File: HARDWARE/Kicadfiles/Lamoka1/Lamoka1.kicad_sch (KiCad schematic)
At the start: 8 parts, among them J1 2606-1108/010-000, J2 2606-1352, J3 USB_C_Receptacle_USB2.0_14P, J4 470531000, J5 2604-1103, J6 Male-Header, J7 Male-Header

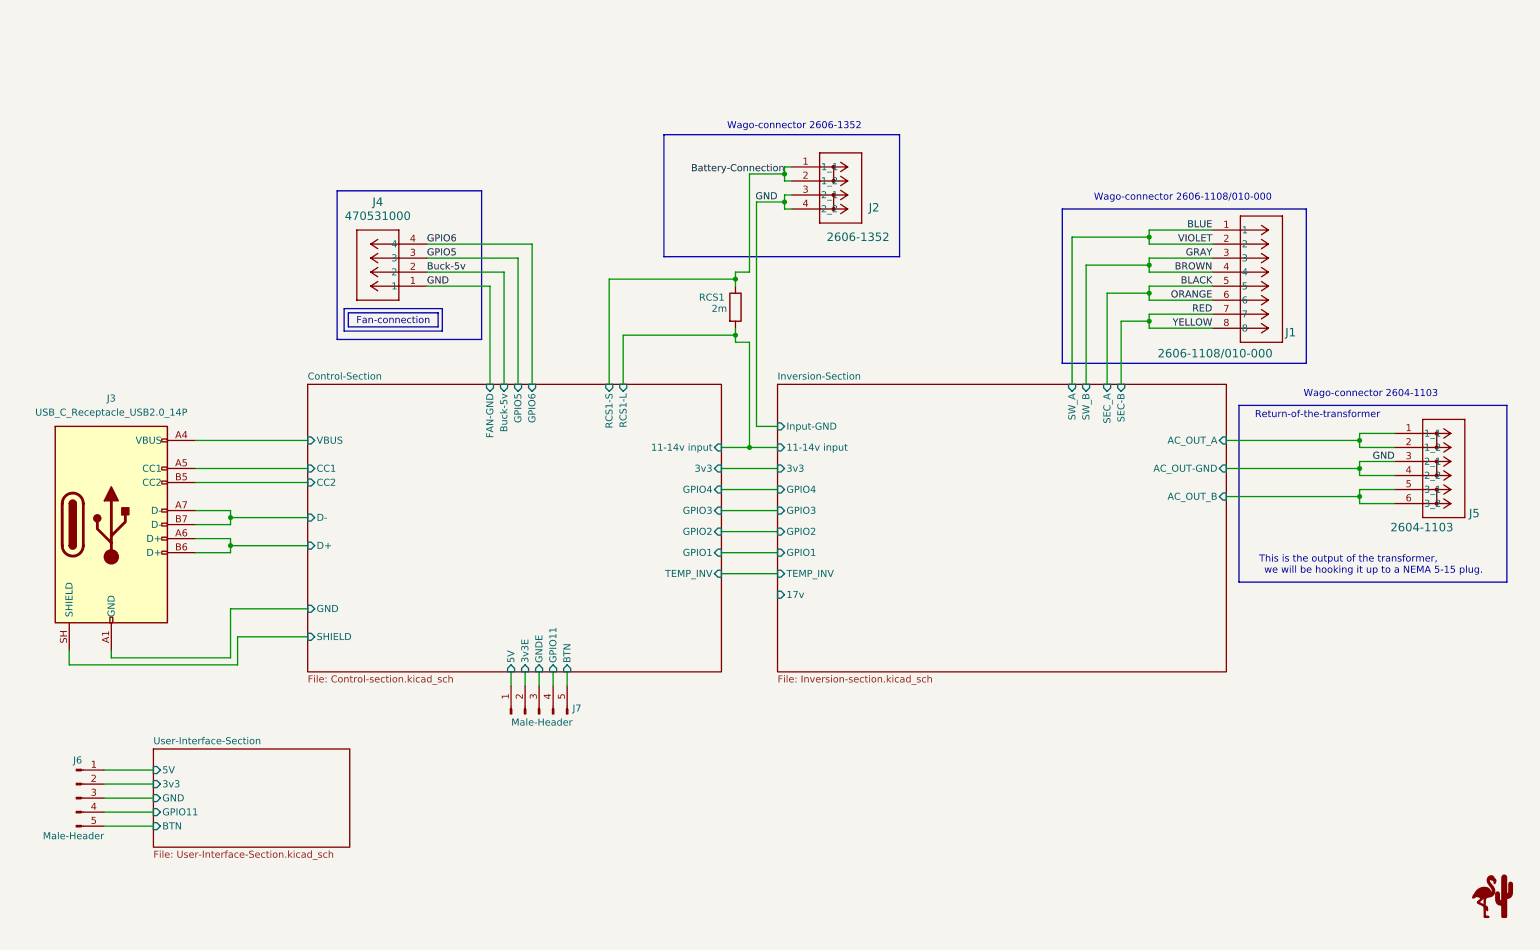
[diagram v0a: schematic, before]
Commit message: ADD H bridge section, tighten everything in PCB routing to be neater. ADD mounting holes M3, etc
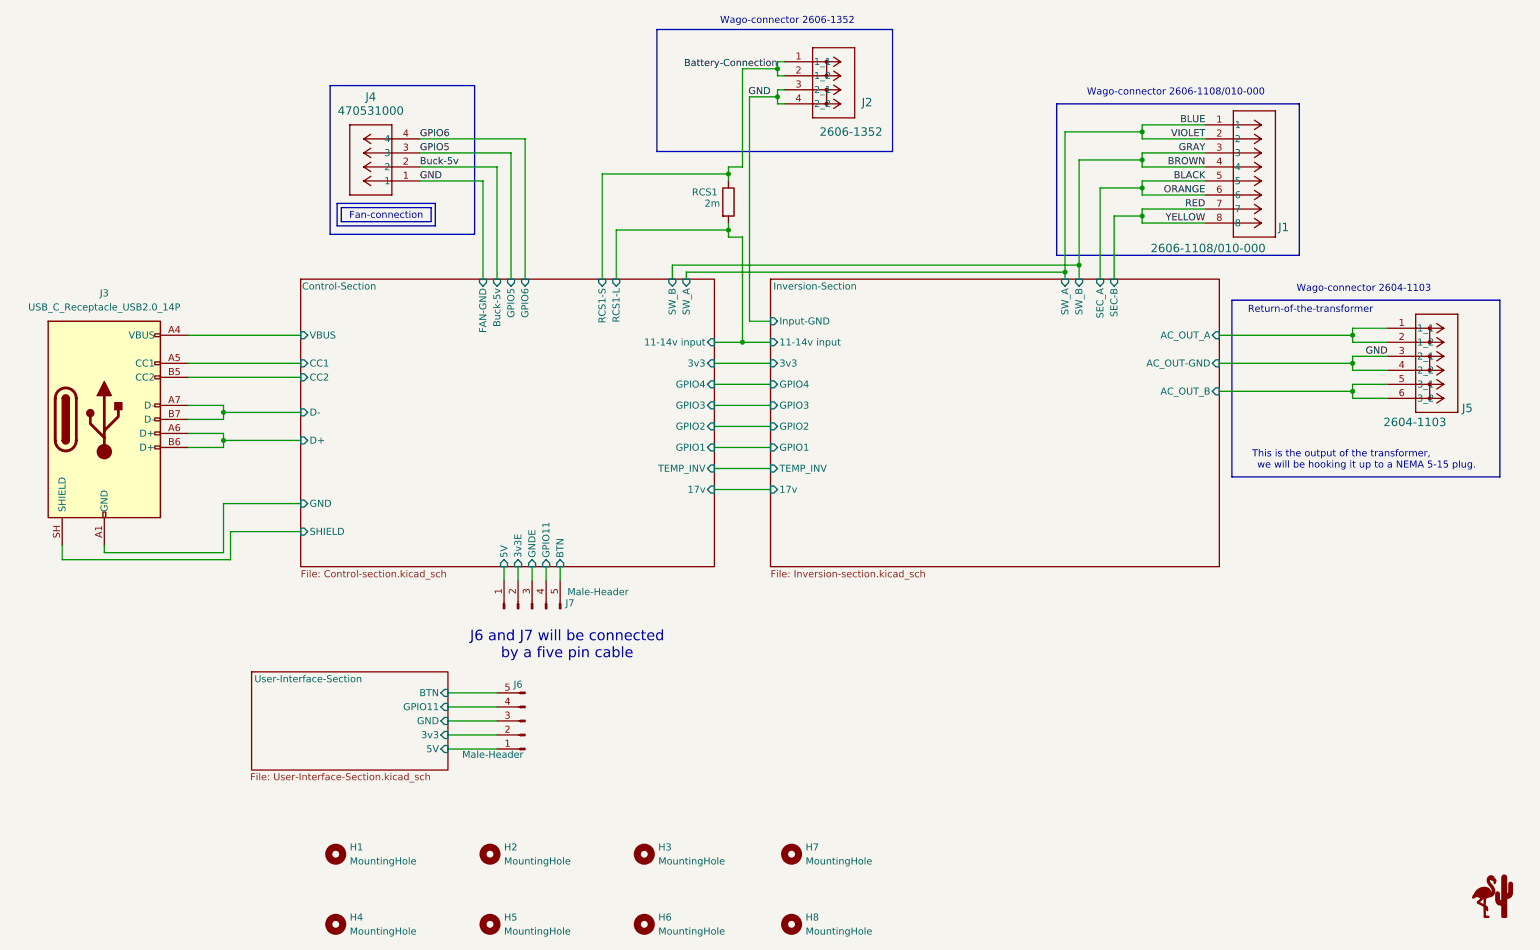
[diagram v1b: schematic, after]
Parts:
- added H1, H2, H3, H4, H5, H6, H7, H8: MountingHole, MountingHole:MountingHole_3.2mm_M3, symbol Mechanical:MountingHole
- J4: footprint 470531000:CONN_SD-47053-001_H10p00_MOL -> Connector:FanPinHeader_1x04_P2.54mm_Vertical
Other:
- sheet Control-Section ports: added 17v, SW_A, SW_B; removed none
- note added: "J6 and J7 will be connected by a five pin cable"
- moved on the sheet: J1, J2, J3, J4, J5, J6, J7, RCS1

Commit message: Get DRC down all the way, other misc improvements
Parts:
- H1, H2, H3, H4, H5, H6, H7, H8: KiLib_Generator (none) -> mounting_hardware/mounting_hole
- J6, J7: KiLib_Generator (none) -> connector/pin_header_socket
- RCS1: KiLib_Generator (none) -> SMD_2terminal_chip_molded
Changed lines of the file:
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@@
+			)
+		)
+		(property "KiLib_Generator" "mounting_hardware/mounting_hole"
+			(at 69.85 167.64 0)
+			(hide yes)
+			(show_name no)
+			(do_not_autoplace no)
+			(effects
+				(font
+					(size 1.27 1.27)
+				)
 			)
 		)
@@
 			)
 		)
+		(property "KiLib_Generator" "mounting_hardware/mounting_hole"
+			(at 152.4 167.64 0)
+			(hide yes)
+			(show_name no)
+			(do_not_autoplace no)
+			(effects
+				(font
+					(size 1.27 1.27)
+				)
+			)
+		)
 		(instances
 			(project "Lamoka1"
@@
 			)
 		)
+		(property "KiLib_Generator" "mounting_hardware/mounting_hole"
+			(at 152.4 180.34 0)
+			(hide yes)
+			(show_name no)
+			(do_not_autoplace no)
+			(effects
+				(font
+					(size 1.27 1.27)
+				)
+			)
+		)
 		(instances
 			(project "Lamoka1"
@@
 			)
 		)
+		(property "KiLib_Generator" "connector/pin_header_socket"
+			(at 104.14 143.51 0)
+			(hide yes)
+			(show_name no)
+			(do_not_autoplace no)
+			(effects
+				(font
+					(size 1.27 1.27)
+				)
+			)
+		)
 		(pin "5"
 		)
@@
 		)
 		(property "Description" "Generic connector, single row, 01x05, script generated"
+			(at 105.41 123.19 0)
+			(hide yes)
+			(show_name no)
+			(do_not_autoplace no)
+			(effects
+				(font
+					(size 1.27 1.27)
+				)
+			)
+		)
+		(property "KiLib_Generator" "connector/pin_header_socket"
 			(at 105.41 123.19 0)
 			(hide yes)
@@
 			)
 		)
+		(property "KiLib_Generator" "mounting_hardware/mounting_hole"
+			(at 97.79 167.64 0)
+			(hide yes)
+			(show_name no)
+			(do_not_autoplace no)
+			(effects
+				(font
+					(size 1.27 1.27)
+				)
+			)
+		)
 		(instances
 			(project "Lamoka1"
@@
 			)
 		)
+		(property "KiLib_Generator" "mounting_hardware/mounting_hole"
+			(at 125.73 180.34 0)
+			(hide yes)
+			(show_name no)
+			(do_not_autoplace no)
+			(effects
+				(font
+					(size 1.27 1.27)
+				)
+			)
+		)
 		(instances
 			(project "Lamoka1"
@@
 		)
 		(property "KLC_S4.2_VREG_LX" ""
+			(at 140.97 49.53 0)
+			(hide yes)
+			(show_name no)
+			(do_not_autoplace no)
+			(effects
+				(font
+					(size 1.27 1.27)
+				)
+			)
+		)
+		(property "KiLib_Generator" "SMD_2terminal_chip_molded"
 			(at 140.97 49.53 0)
 			(hide yes)
@@
 			)
 		)
+		(property "KiLib_Generator" "mounting_hardware/mounting_hole"
+			(at 125.73 167.64 0)
+			(hide yes)
+			(show_name no)
+			(do_not_autoplace no)
+			(effects
+				(font
+					(size 1.27 1.27)
+				)
+			)
+		)
 		(instances
 			(project "Lamoka1"
@@
 			)
 		)
+		(property "KiLib_Generator" "mounting_hardware/mounting_hole"
+			(at 97.79 180.34 0)
+			(hide yes)
+			(show_name no)
+			(do_not_autoplace no)
+			(effects
+				(font
+					(size 1.27 1.27)
+				)
+			)
+		)
 		(instances
 			(project "Lamoka1"
@@
 			(at 69.85 180.34 0)
 			(hide yes)
+			(show_name no)
+			(do_not_autoplace no)
+			(effects
+				(font
+					(size 1.27 1.27)
+				)
+			)
+		)
+		(property "KiLib_Generator" "mounting_hardware/mounting_hole"
+			(at 69.85 180.34 0)
+			(hide yes)

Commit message: Some more slight improvements, general. ADD picture to main readme, etc
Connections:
- net Battery-Connection  renamed +BATT
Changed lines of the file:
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@@
 	)
 	(rectangle
-		(start 128.016 18.288)
+		(start 139.7 18.288)
 		(end 170.688 40.386)
 		(stroke
@@
 	(text "Wago-connector 2606-1352"
 		(exclude_from_sim no)
-		(at 151.638 16.764 0)
+		(at 155.194 16.51 0)
 		(effects
 			(font
@@
 	)
 	(junction
+		(at 143.51 25.4)
+		(diameter 0)
+		(color 0 0 0 0)
+	)
+	(junction
 		(at 254 73.66)
 		(diameter 0)
@@
 		)
 	)
-	(label "Battery-Connection "
-		(at 149.86 25.4 180)
-		(effects
-			(font
-				(size 1.27 1.27)
-			)
-			(justify right bottom)
-		)
-	)
 	(label "BLACK"
 		(at 227.33 45.72 180)
@@
 		)
 		(property "Value" "2606-1352"
-			(at 157.48 36.83 0)
+			(at 153.416 36.068 0)
 			(show_name no)
 			(do_not_autoplace no)
@@
 					(unit 1)
 				)
+			)
+		)
+	)
+	(symbol
+		(lib_id "power:+BATT")
+		(at 143.51 25.4 0)
+		(unit 1)
+		(body_style 1)
+		(exclude_from_sim no)
+		(in_bom yes)
+		(on_board yes)
+		(in_pos_files yes)
+		(dnp no)
+		(fields_autoplaced yes)
+		(property "Reference" "#PWR046"
+			(at 143.51 29.21 0)
+			(hide yes)
+			(show_name no)
+			(do_not_autoplace no)
+			(effects
+				(font
+					(size 1.27 1.27)
+				)
+			)
+		)
+		(property "Value" "+BATT"
+			(at 143.51 20.32 0)
+			(show_name no)
+			(do_not_autoplace no)
+			(effects
+				(font
+					(size 1.27 1.27)
+				)
+			)
+		)
+		(property "Footprint" ""
+			(at 143.51 25.4 0)
+			(hide yes)
+			(show_name no)
+			(do_not_autoplace no)
+			(effects
+				(font
+					(size 1.27 1.27)
+				)
+			)
+		)
+		(property "Datasheet" ""
+			(at 143.51 25.4 0)
+			(hide yes)
+			(show_name no)
+			(do_not_autoplace no)
+			(effects
+				(font
+					(size 1.27 1.27)
+				)
+			)
+		)
+		(property "Description" "Power symbol creates a global label with name \"+BATT\""
+			(at 143.51 25.4 0)
+			(hide yes)
+			(show_name no)
+			(do_not_autoplace no)
+			(effects
+				(font
+					(size 1.27 1.27)
+				)
+			)
+		)
+		(pin "1"
+		)
+		(instances
+			(project "Lamoka1"
+				(path "/c7bb62b6-932f-49c1-a356-0286e905fc0a"
+					(reference "#PWR046")
+					(unit 1)
+				)

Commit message: misc fixes
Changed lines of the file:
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@@
+		)
+	)
+	(symbol
+		(lib_id "power:PWR_FLAG")
+		(at 118.11 44.45 0)
+		(unit 1)
+		(body_style 1)
+		(exclude_from_sim no)
+		(in_bom yes)
+		(on_board yes)
+		(in_pos_files yes)
+		(dnp no)
+		(fields_autoplaced yes)
+		(property "Reference" "#FLG01"
+			(at 118.11 44.45 0)
+			(hide yes)
+			(show_name no)
+			(do_not_autoplace no)
+			(effects
+				(font
+					(size 1.27 1.27)
+				)
+			)
+		)
+		(property "Value" "PWR_FLAG"
+			(at 118.11 44.45 0)
+			(hide yes)
+			(show_name no)
+			(do_not_autoplace no)
+			(effects
+				(font
+					(size 1.27 1.27)
+				)
+			)
+		)
+		(property "Footprint" ""
+			(at 118.11 44.45 0)
+			(hide yes)
+			(show_name no)
+			(do_not_autoplace no)
+			(effects
+				(font
+					(size 1.27 1.27)
+				)
+			)
+		)
+		(property "Datasheet" ""
+			(at 118.11 44.45 0)
+			(hide yes)
+			(show_name no)
+			(do_not_autoplace no)
+			(effects
+				(font
+					(size 1.27 1.27)
+				)
+			)
+		)
+		(property "Description" "Special symbol for telling ERC where power comes from"
+			(at 118.11 44.45 0)
+			(hide yes)
+			(show_name no)
+			(do_not_autoplace no)
+			(effects
+				(font
+					(size 1.27 1.27)
+				)
+			)
+		)
+		(pin "1"
+		)
+		(instances
+			(project "Lamoka1"
+				(path "/c7bb62b6-932f-49c1-a356-0286e905fc0a"
+					(reference "#FLG01")
+					(unit 1)
+				)
+			)
 		)
 	)

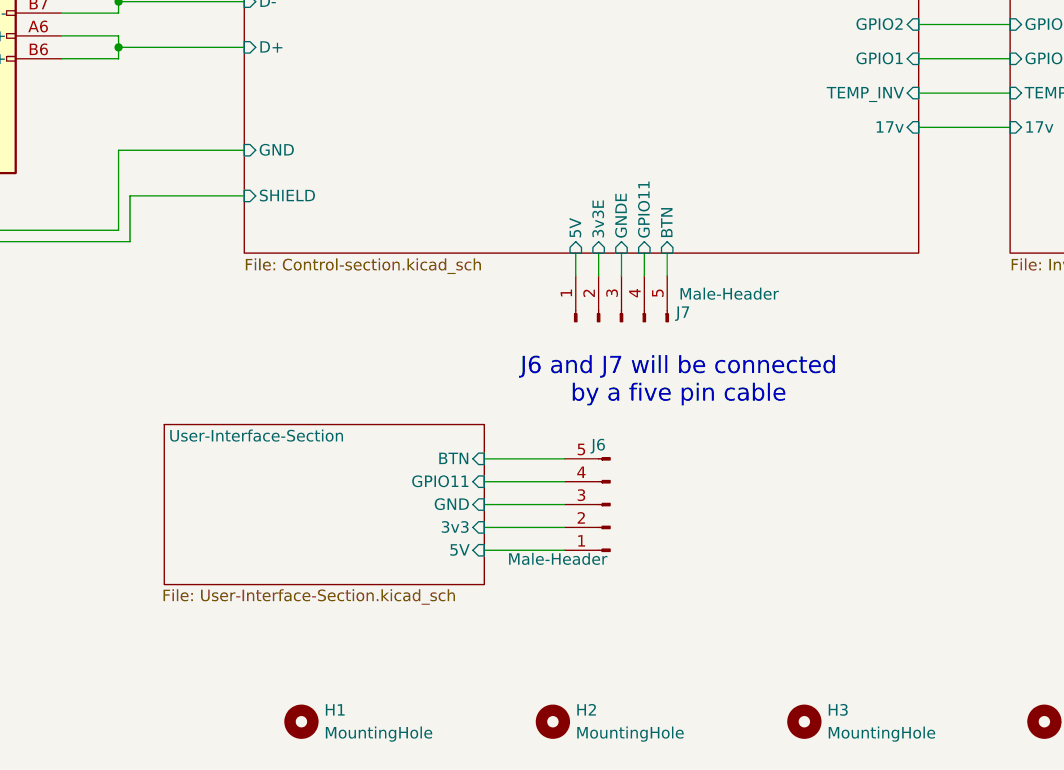
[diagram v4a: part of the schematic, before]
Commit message: major reform on the size of the Lamoka1/2
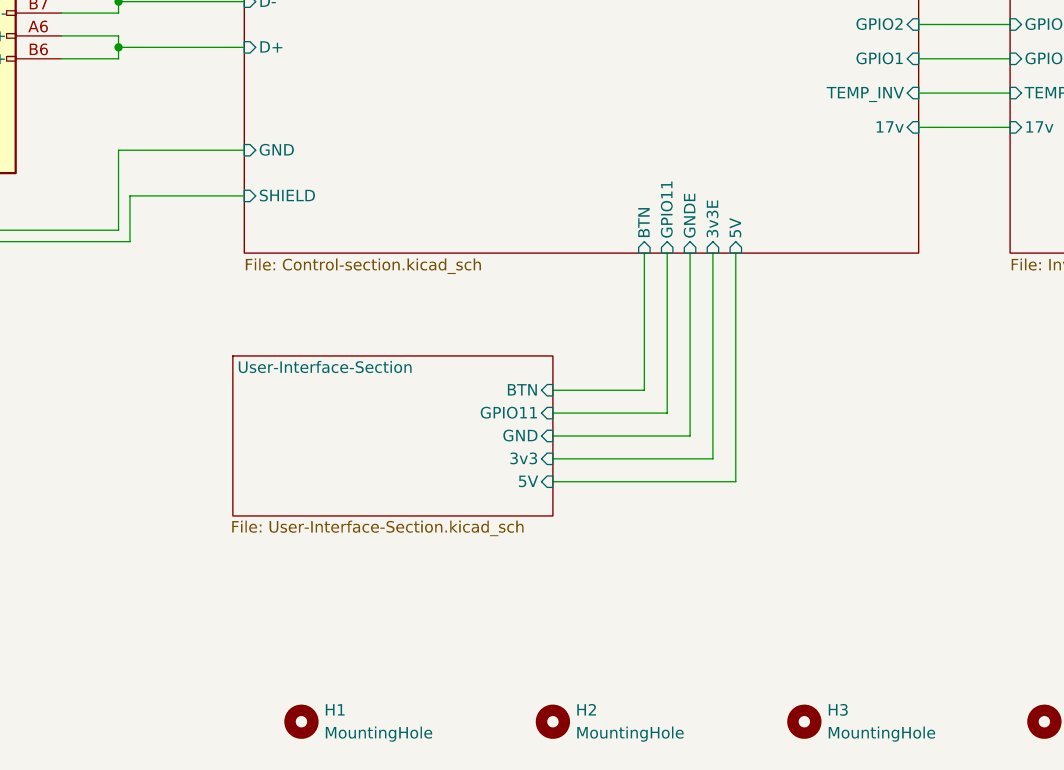
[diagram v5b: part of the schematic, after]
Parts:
- removed J6, J7: Male-Header, Connector_PinHeader_2.54mm:PinHeader_1x05_P2.54mm_Vertical_SMD_Pin1Left, symbol Connector:Conn_01x05_Pin
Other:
- note removed: "J6 and J7 will be connected by a five pin cable"

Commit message: more routing
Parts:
- removed H3, H4, H5, H6, H7, H8: MountingHole, MountingHole:MountingHole_3.2mm_M3, symbol Mechanical:MountingHole

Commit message: MOSFET ROUTING, AND SUCH
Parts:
- removed J4: 470531000, Connector:FanPinHeader_1x04_P2.54mm_Vertical, symbol 470531000:470531000
- added J4: FAN GND, Connector_Wire:SolderWirePad_1x01_SMD_3x6mm, symbol Connector:Conn_01x01_Pin
- added J6: FAN 5V, Connector_Wire:SolderWirePad_1x01_SMD_3x6mm, symbol Connector:Conn_01x01_Pin
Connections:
- new net Control-Section/Buck-5v: J6.1 (Pin_1)
- new net Control-Section/FAN-GND: J4.1 (Pin_1)
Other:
- sheet Control-Section ports: added none; removed GPIO5, GPIO6
- note removed: "Fan-connection"

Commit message: finishing up routing and all of the lamoka1/2
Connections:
- net Control-Section/SHIELD is gone; now on net Control-Section/GND: J3.SH (SHIELD)
- net Control-Section/GND: no longer J3.A1 (GND), J3.A12 (GND), J3.B1 (GND), J3.B12 (GND)
- net Control-Section/11-14v input renamed Control-Section/CSP
- net Control-Section/FAN-GND renamed Control-Section/GND
- net Control-Section/VBUS renamed Control-Section/USB-5v
- new net Control-Section/GND: J3.A1 (GND), J3.A12 (GND), J3.B1 (GND), J3.B12 (GND)
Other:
- sheet Control-Section ports: added CSP, G4D, G4S, Q3S, USB-5v; removed 11-14v input, 17v, 3v3E, FAN-GND, GNDE, SHIELD, SW_A, SW_B, VBUS
- sheet Inversion-Section ports: added CSP, G4D, G4S, GND, Q3S; removed 11-14v input, 17v, AC_OUT-GND, Input-GND, SEC-B, SEC_A, SW_A, SW_B
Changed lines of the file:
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@@
 		)
 	)
-	(label "VIOLET"
+	(label "BLUE"
 		(at 227.33 38.1 180)
 		(effects
@@
 		)
 	)
-	(label "ORANGE"
+	(label "BLACK"
 		(at 227.33 48.26 180)
 		(effects
@@
 		)
 	)
-	(label "GRAY"
+	(label "BROWN"
 		(at 227.33 40.64 180)
 		(effects
@@
 		)
 	)
-	(label "YELLOW"
+	(label "RED"
 		(at 227.33 53.34 180)
 		(effects
@@
 			)
 		)
-		(pin "11-14v input" input
+		(pin "CSP" input
 			(at 148.59 74.93 180)
 			(effects
@@
 			)
 		)
-		(pin "Input-GND" input
+		(pin "GND" input
 			(at 148.59 71.12 180)
 			(effects
@@
 			)
 		)
-		(pin "SW_A" input
+		(pin "Q3S" input
 			(at 201.93 63.5 90)
 			(effects
@@
 			)
 		)
-		(pin "SW_B" input
+		(pin "G4S" input
 			(at 204.47 63.5 90)
 			(effects
@@
 			)
 		)
-		(pin "SEC-B" input
+		(pin "AC_OUT_B" input
 			(at 210.82 63.5 90)
 			(effects
@@
 			)
 		)
-		(pin "SEC_A" input
+		(pin "AC_OUT_A" input
 			(at 208.28 63.5 90)
 			(effects
@@
 			)
 		)
-		(pin "AC_OUT-GND" input
+		(pin "GND" input
 			(at 229.87 78.74 0)
 			(effects
@@
 			)
 		)
-		(pin "17v" input
+		(pin "G4D" input
 			(at 148.59 101.6 180)
 			(effects
@@
 			)
 		)
-		(pin "11-14v input" input
+		(pin "CSP" input
 			(at 138.43 74.93 0)
 			(effects
@@
 			)
 		)
-		(pin "VBUS" input
+		(pin "USB-5v" input
 			(at 63.5 73.66 180)
 			(effects
@@
 			)
 		)
-		(pin "SHIELD" input
+		(pin "GND" input
 			(at 63.5 109.22 180)
 			(effects
@@
 			)
 		)
-		(pin "FAN-GND" input
+		(pin "GND" input
 			(at 96.52 63.5 90)
 			(effects
@@
 			)
 		)
-		(pin "17v" input
+		(pin "G4D" input
 			(at 138.43 101.6 0)
 			(effects
@@
 			)
 		)
-		(pin "SW_A" input
+		(pin "Q3S" input
 			(at 133.35 63.5 90)
 			(effects
@@
 			)
 		)
-		(pin "SW_B" input
+		(pin "G4S" input
 			(at 130.81 63.5 90)
 			(effects
@@
 			)
 		)
-		(pin "3v3E" input
+		(pin "3v3" input
 			(at 115.57 115.57 270)
 			(effects
@@
 			)
 		)
-		(pin "GNDE" input
+		(pin "GND" input
 			(at 113.03 115.57 270)
 			(effects
